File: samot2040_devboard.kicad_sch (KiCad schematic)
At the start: 36 parts, among them J1 USB_C_Receptacle_USB2.0_16P, J2 Conn_01x20, J3 Conn_01x20, J4 Conn_01x03, SW1 SW_Push, SW2 SW_Push, U1 RP2040, U2 MCP1700x-330xxTT, U3 MX25L6433FM2I-08G, Y1 12 MHz

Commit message: upload
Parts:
- removed J4: Conn_01x03, Connector_PinHeader_2.54mm:PinHeader_1x03_P2.54mm_Vertical, symbol Connector_Generic:Conn_01x03
- C1, C10, C11, C12, C17, C18, C2, C3, C4, C5, C6, C7, C8, C9: footprint Capacitor_SMD:C_0603_1608Metric_Pad1.08x0.95mm_HandSolder -> Capacitor_SMD:C_0402_1005Metric_Pad0.74x0.62mm_HandSolder
- R3, R4: footprint Resistor_SMD:R_0603_1608Metric_Pad0.98x0.95mm_HandSolder -> Resistor_SMD:R_0402_1005Metric_Pad0.72x0.64mm_HandSolder
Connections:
- net VBUS: now also J3.1 (Pin_1)
- no-connect marks 7 -> 6
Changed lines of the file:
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@@
 	)
 	(no_connect
-		(at 69.85 123.19)
-	)
-	(no_connect
 		(at 69.85 130.81)
 	)
@@
 	(wire
 		(pts
+			(xy 72.39 121.92) (xy 72.39 123.19)
+		)
+		(stroke
+			(width 0)
+			(type default)
+		)
+	)
+	(wire
+		(pts
 			(xy 154.94 60.96) (xy 154.94 62.23)
 		)
@@
 	(wire
 		(pts
-			(xy 57.15 179.07) (xy 57.15 176.53)
+			(xy 109.22 109.22) (xy 110.49 109.22)
 		)
 		(stroke
@@
 	(wire
 		(pts
-			(xy 109.22 109.22) (xy 110.49 109.22)
+			(xy 35.56 156.21) (xy 40.64 156.21)
 		)
 		(stroke
@@
 	(wire
 		(pts
-			(xy 35.56 156.21) (xy 40.64 156.21)
+			(xy 143.51 73.66) (xy 146.05 73.66)
 		)
 		(stroke
@@
 	(wire
 		(pts
-			(xy 143.51 73.66) (xy 146.05 73.66)
+			(xy 38.1 140.97) (xy 38.1 128.27)
 		)
 		(stroke
@@
 	(wire
 		(pts
-			(xy 38.1 140.97) (xy 38.1 128.27)
+			(xy 125.73 73.66) (xy 123.19 73.66)
 		)
 		(stroke
@@
 	(wire
 		(pts
-			(xy 125.73 73.66) (xy 123.19 73.66)
+			(xy 72.39 123.19) (xy 69.85 123.19)
 		)
 		(stroke
@@
 		)
 	)
-	(global_label "SWD"
-		(shape bidirectional)
-		(at 59.69 176.53 0)
-		(fields_autoplaced yes)
-		(effects
-			(font
-				(size 1.27 1.27)
-			)
-			(justify left)
-		)
-		(property "Intersheetrefs" "${INTERSHEET_REFS}"
-			(at 67.7174 176.53 0)
-			(hide yes)
-			(show_name no)
-			(do_not_autoplace no)
-			(effects
-				(font
-					(size 1.27 1.27)
-				)
-				(justify left)
-			)
-		)
-	)
-	(global_label "SWCLK"
-		(shape bidirectional)
-		(at 54.61 176.53 180)
-		(fields_autoplaced yes)
-		(effects
-			(font
-				(size 1.27 1.27)
-			)
-			(justify right)
-		)
-		(property "Intersheetrefs" "${INTERSHEET_REFS}"
-			(at 44.2845 176.53 0)
-			(hide yes)
-			(show_name no)
-			(do_not_autoplace no)
-			(effects
-				(font
-					(size 1.27 1.27)
-				)
-				(justify right)
-			)
-		)
-	)
 	(global_label "XOUT"
 		(shape input)
@@
 			)
 		)
-		(property "Footprint" "Capacitor_SMD:C_0603_1608Metric_Pad1.08x0.95mm_HandSolder"
+		(property "Footprint" "Capacitor_SMD:C_0402_1005Metric_Pad0.74x0.62mm_HandSolder"
 			(at 143.2052 60.96 0)
 			(hide yes)
@@
 			)
 		)
-		(property "Footprint" "Capacitor_SMD:C_0603_1608Metric_Pad1.08x0.95mm_HandSolder"
+		(property "Footprint" "Capacitor_SMD:C_0402_1005Metric_Pad0.74x0.62mm_HandSolder"
 			(at 121.6152 62.23 0)
 			(hide yes)
@@
 			)
 		)
-		(property "Footprint" "Capacitor_SMD:C_0603_1608Metric_Pad1.08x0.95mm_HandSolder"
+		(property "Footprint" "Capacitor_SMD:C_0402_1005Metric_Pad0.74x0.62mm_HandSolder"
 			(at 149.5552 60.96 0)
 			(hide yes)
@@
 			)
 		)
-		(property "Footprint" "Resistor_SMD:R_0603_1608Metric_Pad0.98x0.95mm_HandSolder"
+		(property "Footprint" "Resistor_SMD:R_0402_1005Metric_Pad0.72x0.64mm_HandSolder"
 			(at 105.41 108.458 90)
 			(hide yes)
@@
 			)
 		)
-		(property "Footprint" "Capacitor_SMD:C_0603_1608Metric_Pad1.08x0.95mm_HandSolder"
+		(property "Footprint" "Capacitor_SMD:C_0402_1005Metric_Pad0.74x0.62mm_HandSolder"
 			(at 162.2552 60.96 0)
 			(hide yes)
@@
 			)
 		)
-		(property "Footprint" "Resistor_SMD:R_0603_1608Metric_Pad0.98x0.95mm_HandSolder"
+		(property "Footprint" "Resistor_SMD:R_0402_1005Metric_Pad0.72x0.64mm_HandSolder"
 			(at 105.41 110.998 90)
 			(hide yes)
@@
 	(symbol
 		(lib_id "power:GND")
-		(at 57.15 179.07 0)
-		(unit 1)
-		(body_style 1)
-		(exclude_from_sim no)
-		(in_bom yes)
-		(on_board yes)
-		(in_pos_files yes)
-		(dnp no)
-		(fields_autoplaced yes)
-		(property "Reference" "#PWR027"
-			(at 57.15 185.42 0)
-			(hide yes)
-			(show_name no)
-			(do_not_autoplace no)
-			(effects
-				(font
-					(size 1.27 1.27)
-				)
-			)
-		)
-		(property "Value" "GND"
-			(at 57.15 184.15 0)
-			(show_name no)
-			(do_not_autoplace no)
-			(effects
-				(font
-					(size 1.27 1.27)
-				)
-			)
-		)
-		(property "Footprint" ""
-			(at 57.15 179.07 0)
-			(hide yes)
-			(show_name no)
-			(do_not_autoplace no)
-			(effects
-				(font
-					(size 1.27 1.27)
-				)
-			)
-		)
-		(property "Datasheet" ""
-			(at 57.15 179.07 0)
-			(hide yes)
-			(show_name no)
-			(do_not_autoplace no)
-			(effects
-				(font
-					(size 1.27 1.27)
-				)
-			)
-		)
-		(property "Description" "Power symbol creates a global label with name \"GND\" , ground"
-			(at 57.15 179.07 0)
-			(hide yes)
-			(show_name no)
-			(do_not_autoplace no)
-			(effects
-				(font
-					(size 1.27 1.27)
-				)
-			)
-		)
-		(pin "1"
-		)
-		(instances
-			(project "samot2040_devboard"
-				(path "/1ccf3c93-6154-4667-b0d2-a1e6f05a8b64"
-					(reference "#PWR027")
-					(unit 1)
-				)
-			)
-		)
-	)
-	(symbol
-		(lib_id "power:GND")
 		(at 57.15 38.1 0)
 		(unit 1)
@@
 			)
 		)
-		(property "Footprint" "Capacitor_SMD:C_0603_1608Metric_Pad1.08x0.95mm_HandSolder"
+		(property "Footprint" "Capacitor_SMD:C_0402_1005Metric_Pad0.74x0.62mm_HandSolder"
 			(at 174.9552 60.96 0)
 			(hide yes)
@@
 			)
 		)
-		(property "Footprint" "Capacitor_SMD:C_0603_1608Metric_Pad1.08x0.95mm_HandSolder"
+		(property "Footprint" "Capacitor_SMD:C_0402_1005Metric_Pad0.74x0.62mm_HandSolder"
 			(at 168.6052 60.96 0)
 			(hide yes)
@@
 			)
 		)
-		(property "Footprint" "Capacitor_SMD:C_0603_1608Metric_Pad1.08x0.95mm_HandSolder"
+		(property "Footprint" "Capacitor_SMD:C_0402_1005Metric_Pad0.74x0.62mm_HandSolder"
 			(at 108.9152 62.23 0)
 			(hide yes)
@@
 			)
 		)
-		(property "Footprint" "Capacitor_SMD:C_0603_1608Metric_Pad1.08x0.95mm_HandSolder"
+		(property "Footprint" "Capacitor_SMD:C_0402_1005Metric_Pad0.74x0.62mm_HandSolder"
 			(at 155.9052 60.96 0)
 			(hide yes)
@@
 			)
 		)
-		(property "Footprint" "Capacitor_SMD:C_0603_1608Metric_Pad1.08x0.95mm_HandSolder"
+		(property "Footprint" "Capacitor_SMD:C_0402_1005Metric_Pad0.74x0.62mm_HandSolder"
 			(at 187.6552 60.96 0)
 			(hide yes)
@@
 	)
 	(symbol
+		(lib_id "power:VBUS")
+		(at 72.39 121.92 0)
+		(unit 1)
+		(body_style 1)
+		(exclude_from_sim no)
+		(in_bom yes)
+		(on_board yes)
+		(in_pos_files yes)
+		(dnp no)
+		(fields_autoplaced yes)
+		(property "Reference" "#PWR027"
+			(at 72.39 125.73 0)
+			(hide yes)
+			(show_name no)
+			(do_not_autoplace no)
+			(effects
+				(font
+					(size 1.27 1.27)
+				)
+			)
+		)
+		(property "Value" "VBUS"
+			(at 72.39 116.84 0)
+			(show_name no)
+			(do_not_autoplace no)
+			(effects
+				(font
+					(size 1.27 1.27)
+				)
+			)
+		)
+		(property "Footprint" ""
+			(at 72.39 121.92 0)
+			(hide yes)
+			(show_name no)
+			(do_not_autoplace no)
+			(effects
+				(font
+					(size 1.27 1.27)
+				)
+			)
+		)
+		(property "Datasheet" ""
+			(at 72.39 121.92 0)
+			(hide yes)
+			(show_name no)
+			(do_not_autoplace no)
+			(effects
+				(font
+					(size 1.27 1.27)
+				)
+			)
+		)
+		(property "Description" "Power symbol creates a global label with name \"VBUS\""
+			(at 72.39 121.92 0)
+			(hide yes)
+			(show_name no)
+			(do_not_autoplace no)
+			(effects
+				(font
+					(size 1.27 1.27)
+				)
+			)
+		)
+		(pin "1"
+		)
+		(instances
+			(project "samot2040_devboard"
+				(path "/1ccf3c93-6154-4667-b0d2-a1e6f05a8b64"
+					(reference "#PWR027")
+					(unit 1)
+				)
+			)
+		)
+	)
+	(symbol
 		(lib_id "power:GND")
 		(at 114.3 67.31 0)
@@
 			)
 		)
-		(property "Footprint" "Capacitor_SMD:C_0603_1608Metric_Pad1.08x0.95mm_HandSolder"
+		(property "Footprint" "Capacitor_SMD:C_0402_1005Metric_Pad0.74x0.62mm_HandSolder"
 			(at 136.8552 60.96 0)
 			(hide yes)
@@
 			)
 		)
-		(property "Footprint" "Capacitor_SMD:C_0603_1608Metric_Pad1.08x0.95mm_HandSolder"
+		(property "Footprint" "Capacitor_SMD:C_0402_1005Metric_Pad0.74x0.62mm_HandSolder"
 			(at 115.2652 62.23 0)
 			(hide yes)
@@
 			)
 		)
-		(property "Footprint" "Capacitor_SMD:C_0603_1608Metric_Pad1.08x0.95mm_HandSolder"
+		(property "Footprint" "Capacitor_SMD:C_0402_1005Metric_Pad0.74x0.62mm_HandSolder"
 			(at 257.81 79.0448 0)
 			(hide yes)
@@
 			)
 		)
-		(property "Footprint" "Capacitor_SMD:C_0603_1608Metric_Pad1.08x0.95mm_HandSolder"
+		(property "Footprint" "Capacitor_SMD:C_0402_1005Metric_Pad0.74x0.62mm_HandSolder"
 			(at 96.2152 96.52 0)
 			(hide yes)
@@
 			)
 		)
-		(property "Footprint" "Capacitor_SMD:C_0603_1608Metric_Pad1.08x0.95mm_HandSolder"
+		(property "Footprint" "Capacitor_SMD:C_0402_1005Metric_Pad0.74x0.62mm_HandSolder"
 			(at 181.3052 60.96 0)
 			(hide yes)
@@
 					(unit 1)
 				)
-			)
-		)
-	)
-	(symbol
-		(lib_id "Connector_Generic:Conn_01x03")
-		(at 57.15 171.45 90)
-		(unit 1)
-		(body_style 1)
-		(exclude_from_sim no)
-		(in_bom yes)
-		(on_board yes)
-		(in_pos_files yes)
-		(dnp no)
-		(property "Reference" "J4"
-			(at 55.372 165.862 90)
-			(show_name no)
-			(do_not_autoplace no)
-			(effects
-				(font
-					(size 1.27 1.27)
-				)
-				(justify right)
-			)
-		)
-		(property "Value" "Conn_01x03"
-			(at 50.8 168.402 90)
-			(show_name no)
-			(do_not_autoplace no)
-			(effects
-				(font
-					(size 1.27 1.27)
-				)
-				(justify right)
-			)
-		)
-		(property "Footprint" "Connector_PinHeader_2.54mm:PinHeader_1x03_P2.54mm_Vertical"
-			(at 57.15 171.45 0)
-			(hide yes)
-			(show_name no)
-			(do_not_autoplace no)
-			(effects
-				(font
-					(size 1.27 1.27)
-				)
-			)
-		)
-		(property "Datasheet" ""
-			(at 57.15 171.45 0)
-			(hide yes)
-			(show_name no)
-			(do_not_autoplace no)
-			(effects
-				(font
-					(size 1.27 1.27)
-				)
-			)
-		)
-		(property "Description" "Generic connector, single row, 01x03, script generated (kicad-library-utils/schlib/autogen/connector/)"
-			(at 57.15 171.45 0)
-			(hide yes)
-			(show_name no)
-			(do_not_autoplace no)
-			(effects
-				(font
-					(size 1.27 1.27)
-				)
-			)
-		)
-		(pin "2"
-		)
-		(pin "1"
-		)
-		(pin "3"
-		)
-		(instances
-			(project "samot2040_devboard"
-				(path "/1ccf3c93-6154-4667-b0d2-a1e6f05a8b64"
-					(reference "J4")
-					(unit 1)
-				)

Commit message: added firmware
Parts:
- J1: footprint Connector_USB:USB_C_Receptacle_GCT_USB4085 -> Connector_USB:USB_C_Receptacle_GCT_USB4105-xx-A_16P_TopMnt_Horizontal
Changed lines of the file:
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@@
 			)
 		)
-		(property "Footprint" "Connector_USB:USB_C_Receptacle_GCT_USB4085"
+		(property "Footprint" "Connector_USB:USB_C_Receptacle_GCT_USB4105-xx-A_16P_TopMnt_Horizontal"
 			(at 31.75 45.72 0)
 			(hide yes)

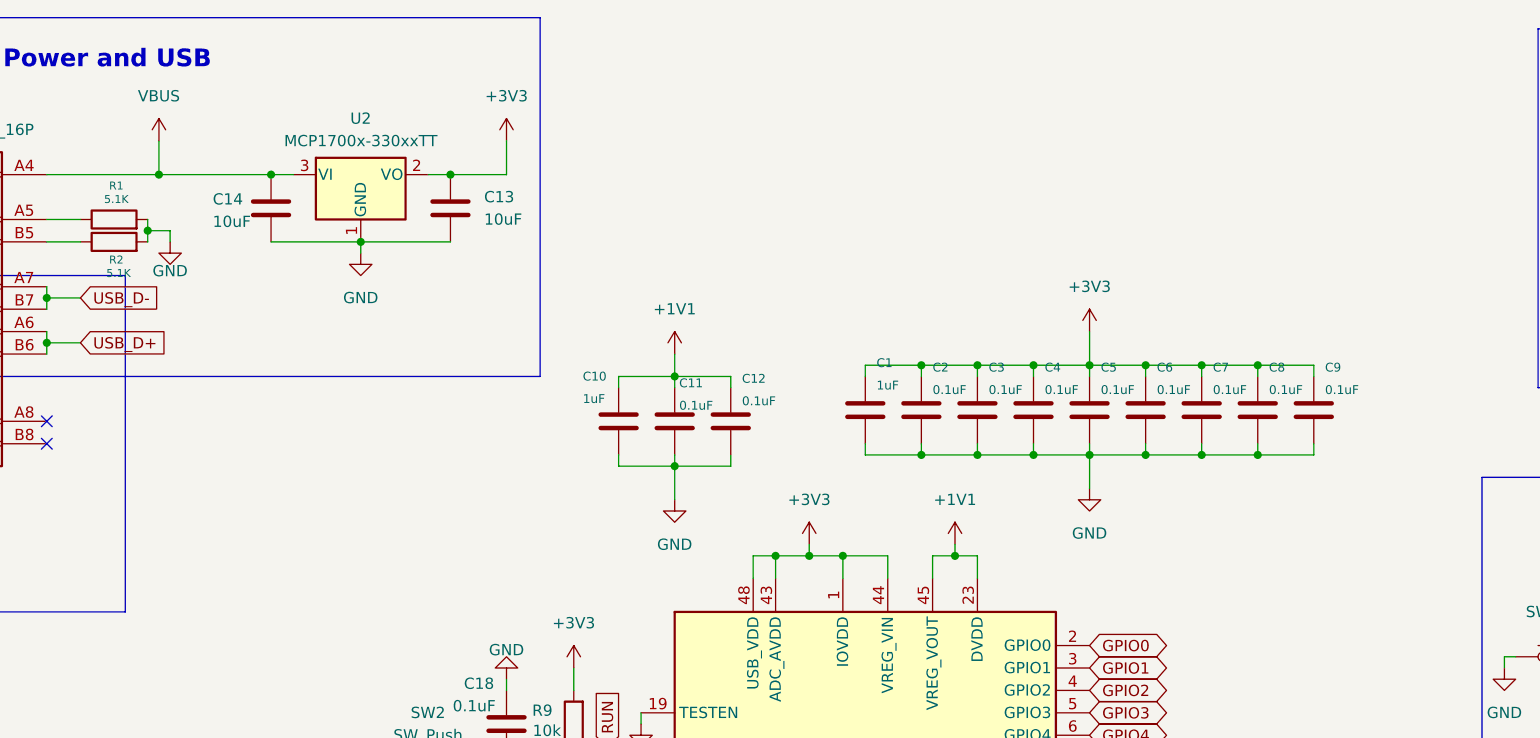
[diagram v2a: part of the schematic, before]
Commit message: added battery support and charging
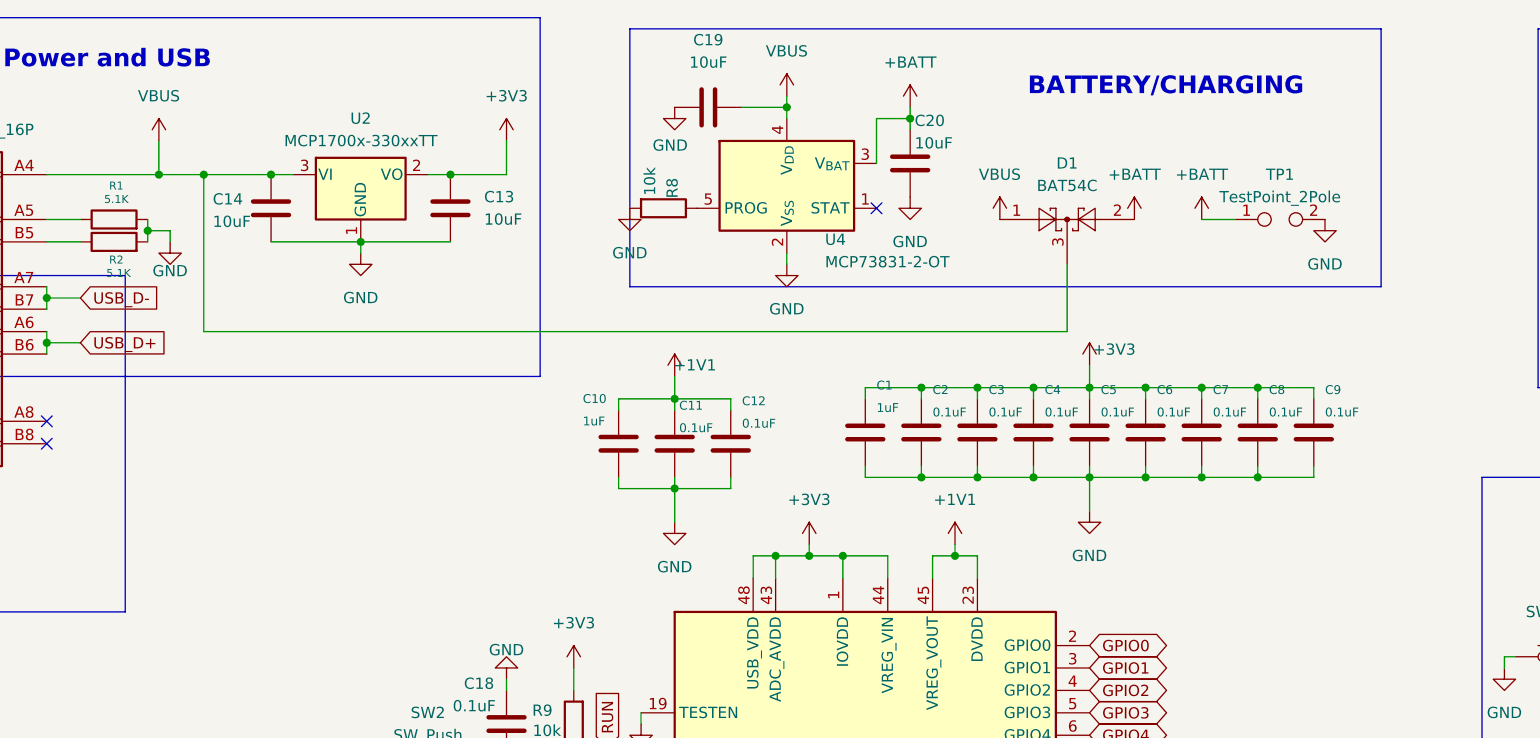
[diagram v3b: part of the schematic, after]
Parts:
- added C19, C20: 10uF, Capacitor_SMD:C_0603_1608Metric_Pad1.08x0.95mm_HandSolder, symbol Device:C
- added D1: BAT54C, Package_TO_SOT_SMD:SOT-23_Handsoldering, symbol Diode:BAT54C
- added R8: 10k, Resistor_SMD:R_0603_1608Metric_Pad0.98x0.95mm_HandSolder, symbol Device:R
- added TP1: TestPoint_2Pole, TestPoint:TestPoint_2Pads_Pitch2.54mm_Drill0.8mm, symbol Connector:TestPoint_2Pole
- added U4: MCP73831-2-OT, Package_TO_SOT_SMD:SOT-23-5_HandSoldering, symbol Battery_Management:MCP73831-2-OT
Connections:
- net GND: now also C19.1, C20.1, R8.2, TP1.2, U4.2 (V_{SS})
- net VBUS: now also C19.2, D1.1, D1.3, U4.4 (V_{DD})
- new net: R8.1, U4.5 (PROG)
- new net +BATT: C20.2, D1.2, TP1.1, U4.3 (V_{BAT})
- no-connect marks 6 -> 7
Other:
- note added: "BATTERY/CHARGING"
- moved on the sheet: C1, C10, C11, C12, C2, C3, C4, C5, C6, C7, C8, C9
